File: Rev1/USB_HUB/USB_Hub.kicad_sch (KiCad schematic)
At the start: 0 parts

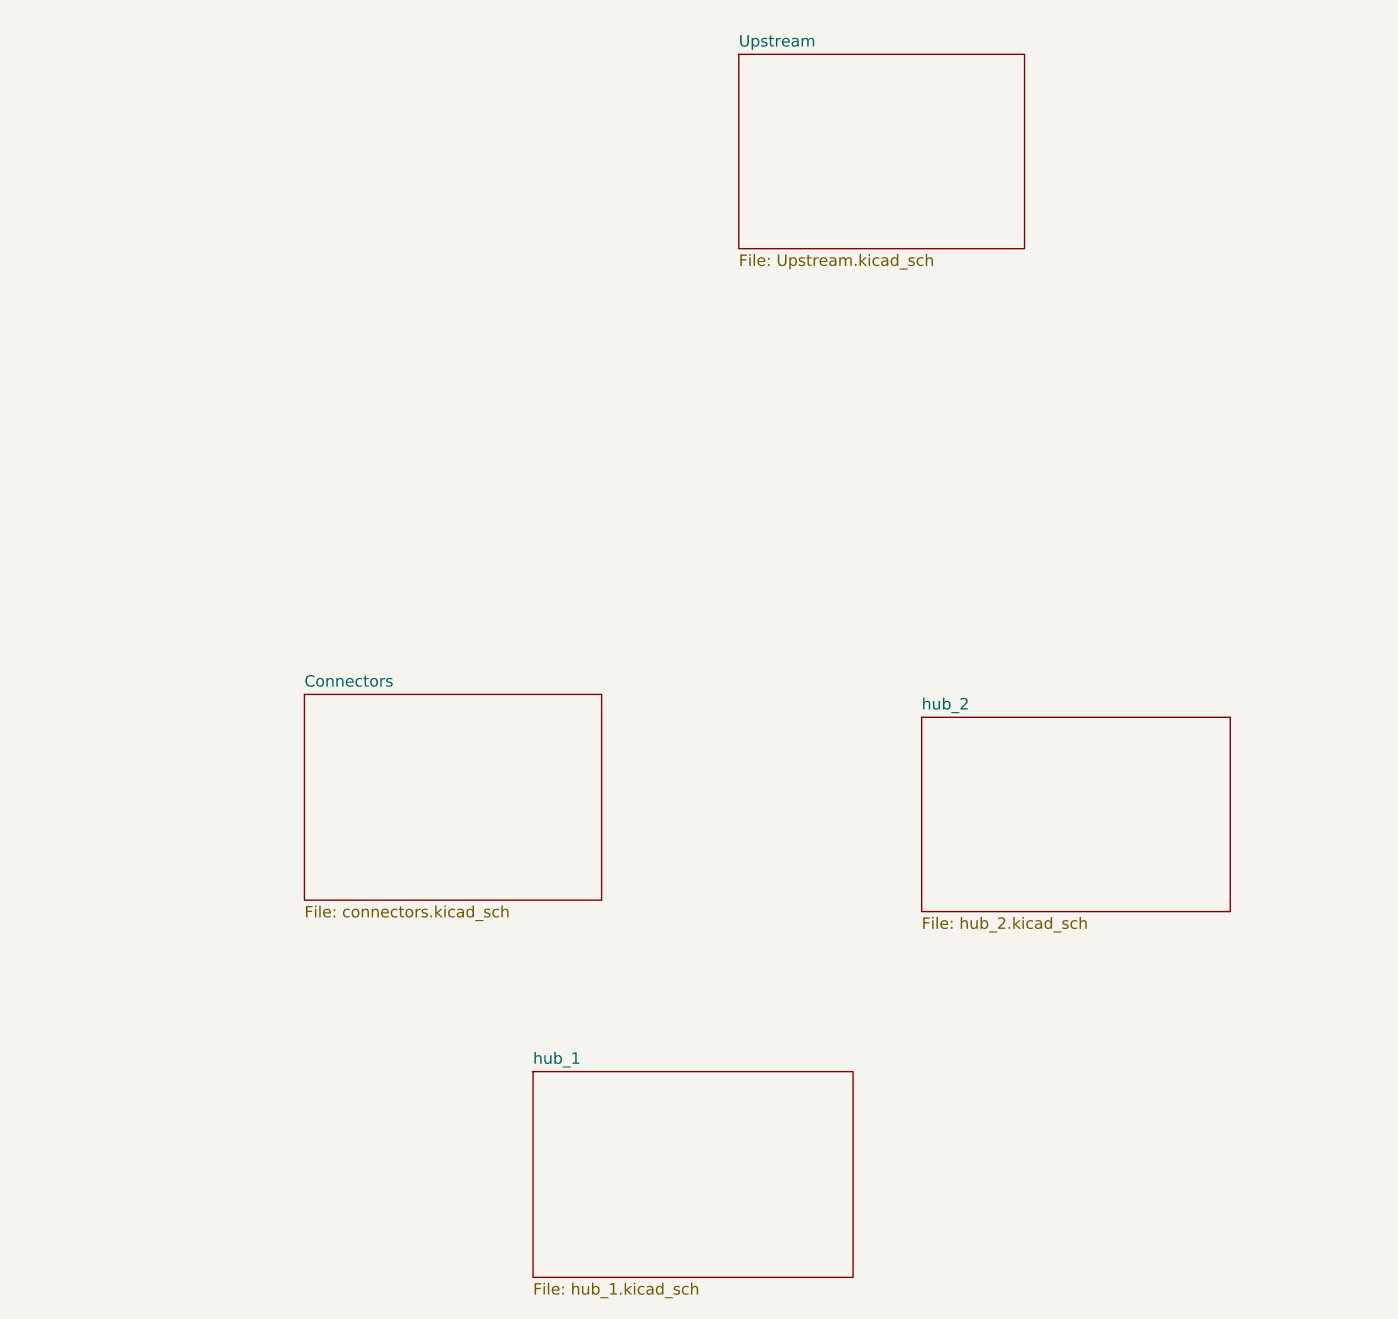
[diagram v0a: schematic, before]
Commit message: USB HUB Updated
Based on TA feedback
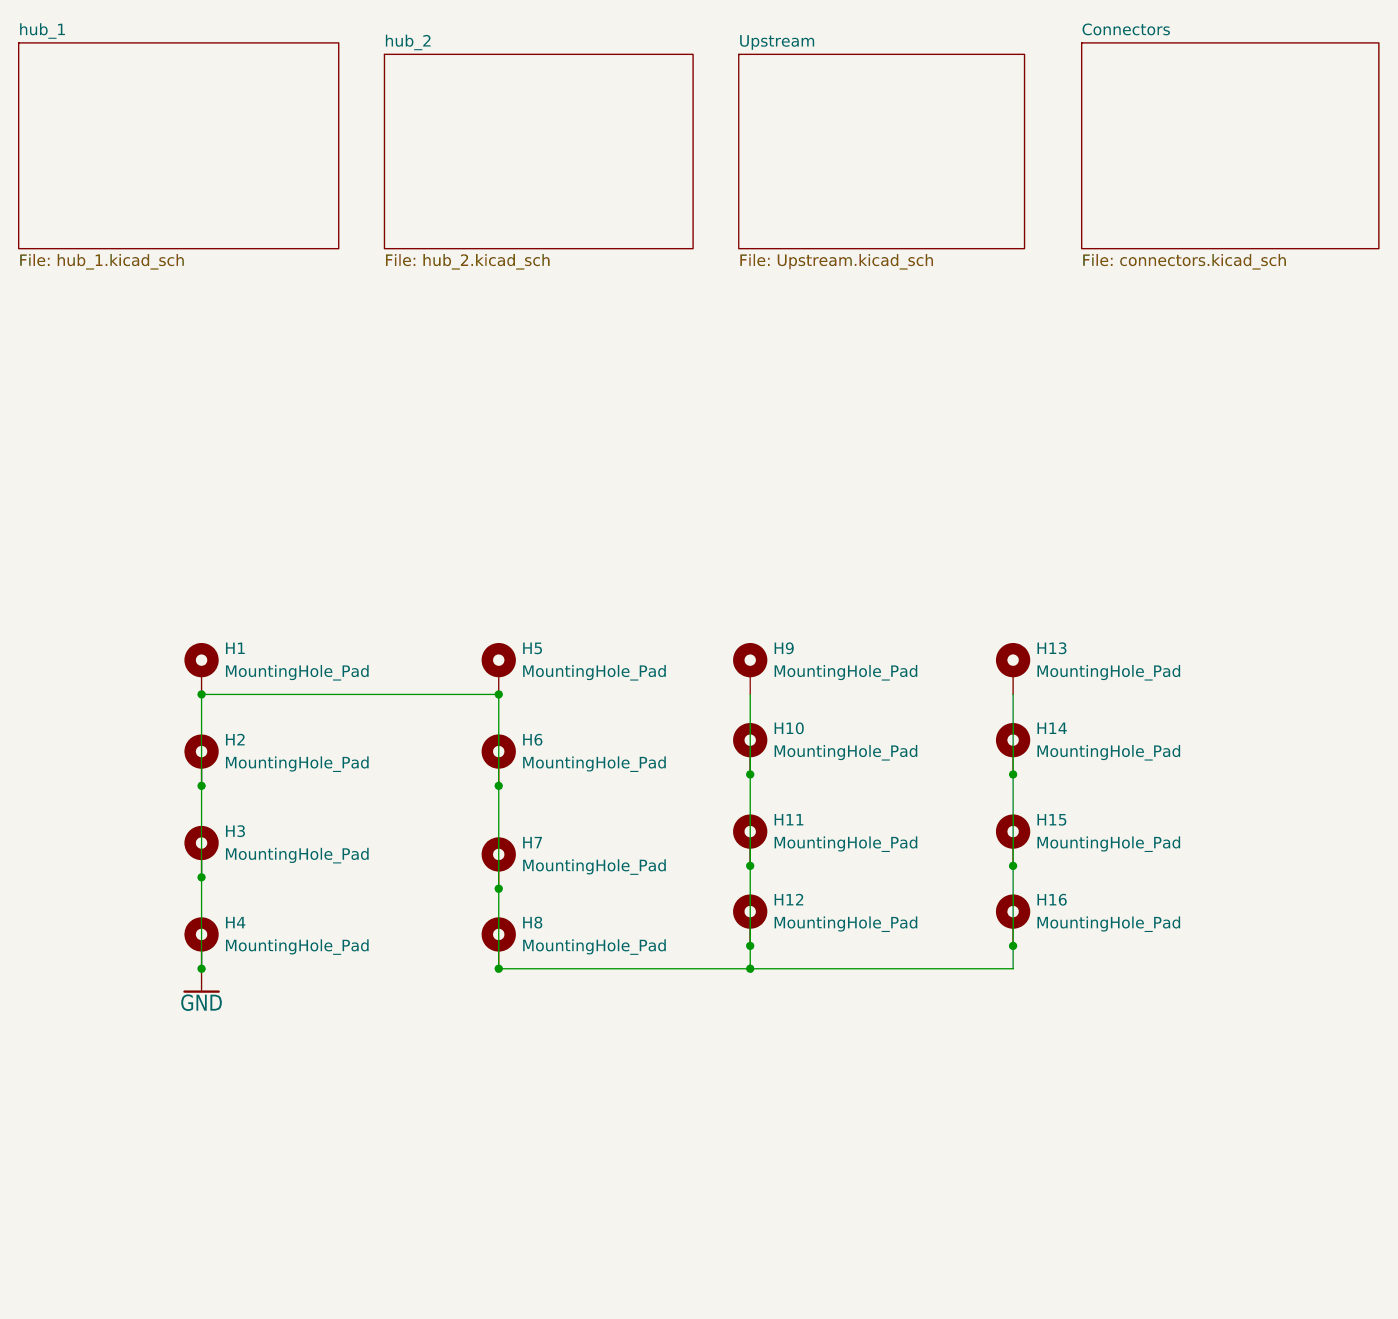
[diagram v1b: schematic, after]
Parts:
- added H1, H2, H3, H4: MountingHole_Pad, MountingHole:MountingHole_3.2mm_M3_DIN965_Pad, symbol Mechanical:MountingHole_Pad
- added H10, H11, H12, H13, H14, H15, H16, H9: MountingHole_Pad, MountingHole:MountingHole_USB, symbol Mechanical:MountingHole_Pad
- added H5, H6, H7, H8: MountingHole_Pad, MountingHole:MountingHole_2.2mm_M2_DIN965_Pad, symbol Mechanical:MountingHole_Pad
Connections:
- new net GND: H1.1, H10.1, H11.1, H12.1, H13.1, H14.1, H15.1, H16.1, H2.1, H3.1, H4.1, H5.1, H6.1, H7.1, H8.1, H9.1
